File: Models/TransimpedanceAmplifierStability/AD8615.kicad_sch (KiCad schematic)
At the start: 10 parts

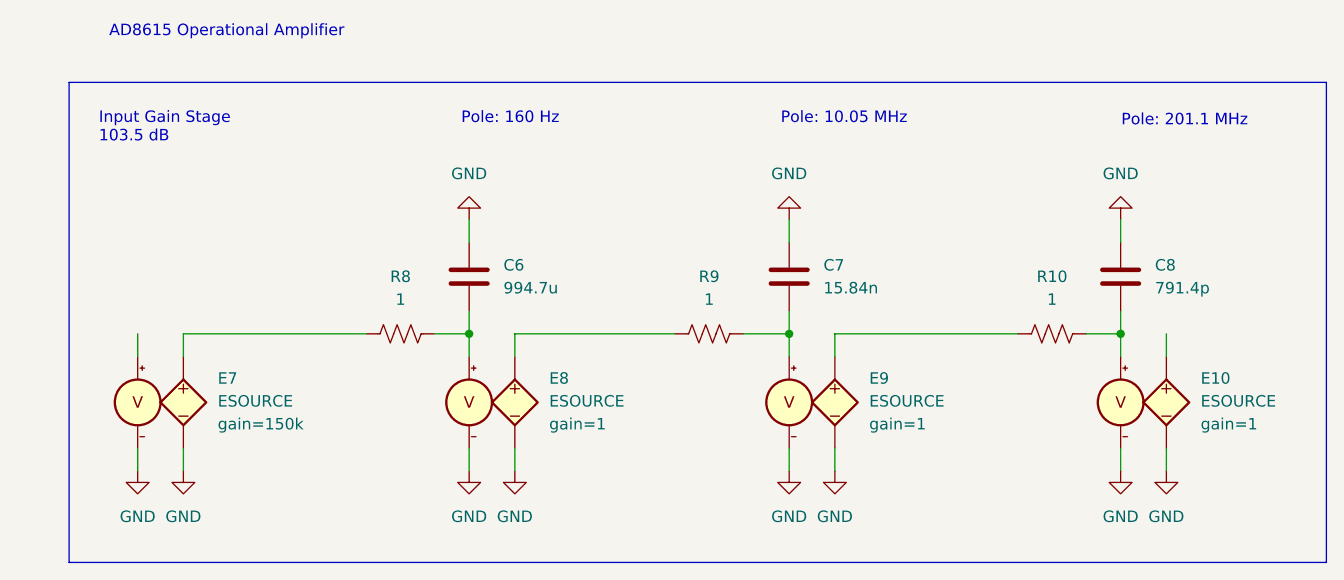
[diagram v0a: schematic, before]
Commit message: Upload completed model of the LTC6090-5
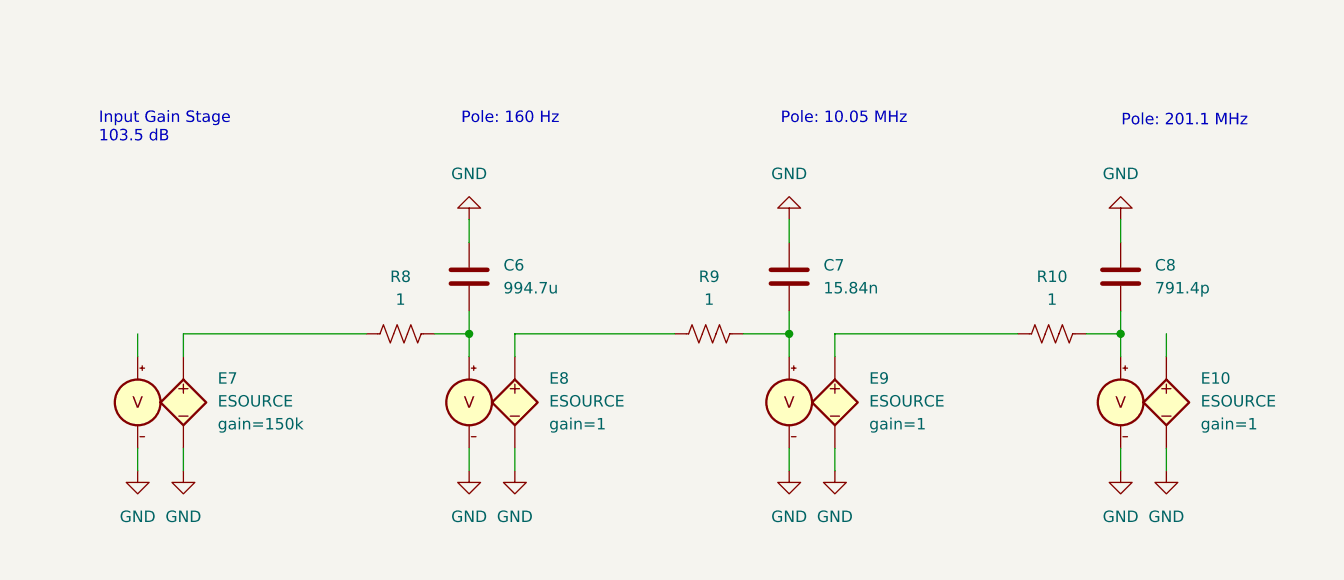
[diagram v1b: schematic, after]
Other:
- note removed: "AD8615 Operational Amplifier"
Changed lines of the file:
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@@
 	(generator_version "9.0")
 	(paper "A4")
-	(rectangle
-		(start 93.98 68.58)
-		(end 233.68 121.92)
-		(stroke
-			(width 0)
-			(type default)
-		)
-		(fill
-			(type none)
-		)
-	)
 	(text "Input Gain Stage\n103.5 dB"
 		(exclude_from_sim no)
@@
 		(effects
 			(font
-				(size 1.27 1.27)
-			)
-		)
-	)
-	(text "AD8615 Operational Amplifier"
-		(exclude_from_sim no)
-		(at 111.506 62.992 0)
-		(effects
-			(font

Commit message: Upload latest version of TIA stability KiCad project
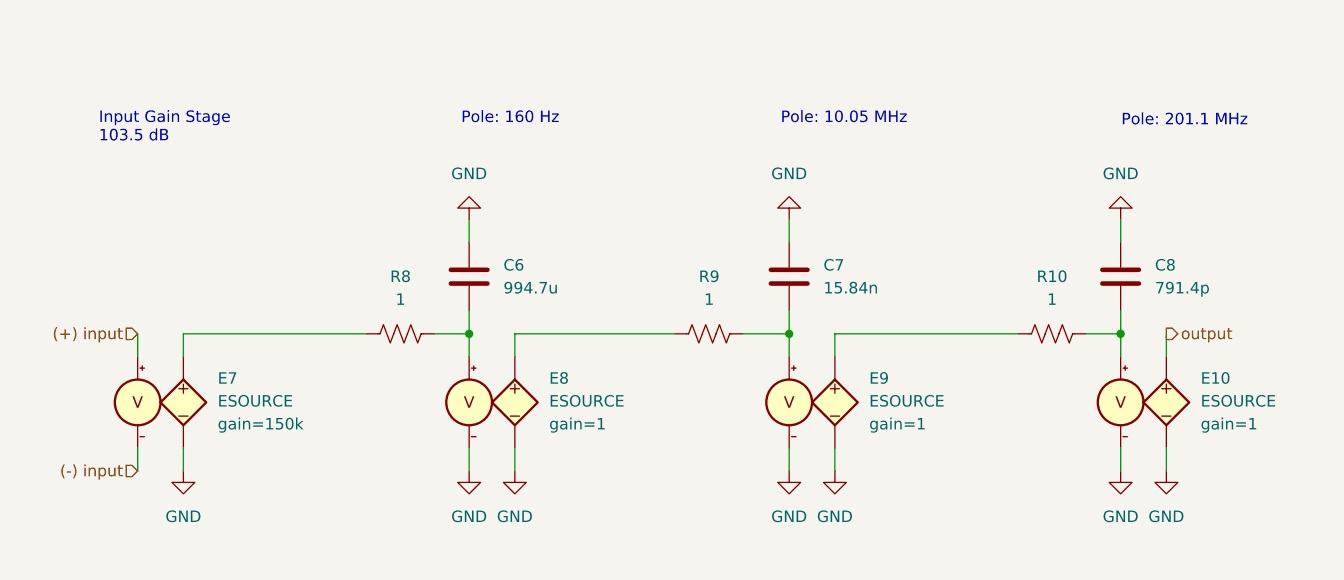
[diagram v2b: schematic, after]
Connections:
- net GND: no longer E7.4 (C-)
- net (+) input: now reaches E7.3 (C+)
- net output: now reaches E10.1 (N+)
- new net (-) input: E7.4 (C-)
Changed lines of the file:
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@@
+		)
+	)
+	(hierarchical_label "output"
+		(shape output)
+		(at 215.9 96.52 0)
+		(effects
+			(font
+				(size 1.27 1.27)
+			)
+			(justify left)
+		)
+	)
+	(hierarchical_label "(-) input"
+		(shape input)
+		(at 101.6 111.76 180)
+		(effects
+			(font
+				(size 1.27 1.27)
+			)
+			(justify right)
+		)
+	)
+	(hierarchical_label "(+) input"
+		(shape input)
+		(at 101.6 96.52 180)
+		(effects
+			(font
+				(size 1.27 1.27)
+			)
+			(justify right)
 		)
 	)
@@
 					(unit 1)
 				)
+				(path "/b282eeea-1083-4bd9-aef5-c78f2e129a69/83a2ffcb-675c-4711-b7ba-b056f35f4220"
+					(reference "#PWR035")
+					(unit 1)
+				)
 			)
 		)
@@
 					(unit 1)
 				)
+				(path "/b282eeea-1083-4bd9-aef5-c78f2e129a69/83a2ffcb-675c-4711-b7ba-b056f35f4220"
+					(reference "E12")
+					(unit 1)
+				)
 			)
 		)
@@
 					(unit 1)
 				)
+				(path "/b282eeea-1083-4bd9-aef5-c78f2e129a69/83a2ffcb-675c-4711-b7ba-b056f35f4220"
+					(reference "#PWR039")
+					(unit 1)
+				)
 			)
 		)
@@
 					(unit 1)
 				)
+				(path "/b282eeea-1083-4bd9-aef5-c78f2e129a69/83a2ffcb-675c-4711-b7ba-b056f35f4220"
+					(reference "#PWR034")
+					(unit 1)
+				)
 			)
 		)
@@
 					(unit 1)
 				)
+				(path "/b282eeea-1083-4bd9-aef5-c78f2e129a69/83a2ffcb-675c-4711-b7ba-b056f35f4220"
+					(reference "C9")
+					(unit 1)
+				)
 			)
 		)
@@
 					(unit 1)
 				)
+				(path "/b282eeea-1083-4bd9-aef5-c78f2e129a69/83a2ffcb-675c-4711-b7ba-b056f35f4220"
+					(reference "R11")
+					(unit 1)
+				)
 			)
 		)
@@
 					(unit 1)
 				)
+				(path "/b282eeea-1083-4bd9-aef5-c78f2e129a69/83a2ffcb-675c-4711-b7ba-b056f35f4220"
+					(reference "#PWR05")
+					(unit 1)
+				)
 			)
 		)
@@
 					(unit 1)
 				)
+				(path "/b282eeea-1083-4bd9-aef5-c78f2e129a69/83a2ffcb-675c-4711-b7ba-b056f35f4220"
+					(reference "#PWR041")
+					(unit 1)
+				)
 			)
 		)
@@
 					(unit 1)
 				)
+				(path "/b282eeea-1083-4bd9-aef5-c78f2e129a69/83a2ffcb-675c-4711-b7ba-b056f35f4220"
+					(reference "#PWR040")
+					(unit 1)
+				)
 			)
 		)
@@
 					(unit 1)
 				)
+				(path "/b282eeea-1083-4bd9-aef5-c78f2e129a69/83a2ffcb-675c-4711-b7ba-b056f35f4220"
+					(reference "#PWR036")
+					(unit 1)
+				)
 			)
 		)
@@
 					(unit 1)
 				)
+				(path "/b282eeea-1083-4bd9-aef5-c78f2e129a69/83a2ffcb-675c-4711-b7ba-b056f35f4220"
+					(reference "E11")
+					(unit 1)
+				)
 			)
 		)
@@
 					(unit 1)
 				)
+				(path "/b282eeea-1083-4bd9-aef5-c78f2e129a69/83a2ffcb-675c-4711-b7ba-b056f35f4220"
+					(reference "#PWR038")
+					(unit 1)
+				)
 			)
 		)
@@
 					(unit 1)
 				)
+				(path "/b282eeea-1083-4bd9-aef5-c78f2e129a69/83a2ffcb-675c-4711-b7ba-b056f35f4220"
+					(reference "R12")
+					(unit 1)
+				)
 			)
 		)
@@
 					(unit 1)
 				)
-			)
-		)
-	)
-	(symbol
-		(lib_id "power:GND")
-		(at 101.6 111.76 0)
-		(unit 1)
-		(exclude_from_sim no)
-		(in_bom yes)
-		(on_board yes)
-		(dnp no)
-		(fields_autoplaced yes)
-		(property "Reference" "#PWR07"
-			(at 101.6 118.11 0)
-			(effects
-				(font
-					(size 1.27 1.27)
-				)
-				(hide yes)
-			)
-		)
-		(property "Value" "GND"
-			(at 101.6 116.84 0)
-			(effects
-				(font
-					(size 1.27 1.27)
-				)
-			)
-		)
-		(property "Footprint" ""
-			(at 101.6 111.76 0)
-			(effects
-				(font
-					(size 1.27 1.27)
-				)
-				(hide yes)
-			)
-		)
-		(property "Datasheet" ""
-			(at 101.6 111.76 0)
-			(effects
-				(font
-					(size 1.27 1.27)
-				)
-				(hide yes)
-			)
-		)
-		(property "Description" "Power symbol creates a global label with name \"GND\" , ground"
-			(at 101.6 111.76 0)
-			(effects
-				(font
-					(size 1.27 1.27)
-				)
-				(hide yes)
-			)
-		)
-		(pin "1"
-		)
-		(instances
-			(project "TransimpedanceAmplifierStability"
-				(path "/b282eeea-1083-4bd9-aef5-c78f2e129a69/350a7392-f8dd-4a96-b4e8-c2f5595b2b98"
-					(reference "#PWR07")
+				(path "/b282eeea-1083-4bd9-aef5-c78f2e129a69/83a2ffcb-675c-4711-b7ba-b056f35f4220"
+					(reference "#PWR037")
 					(unit 1)
 				)
@@
 					(unit 1)
 				)
+				(path "/b282eeea-1083-4bd9-aef5-c78f2e129a69/83a2ffcb-675c-4711-b7ba-b056f35f4220"
+					(reference "E14")
+					(unit 1)
+				)
 			)
 		)
@@
 					(unit 1)
 				)
+				(path "/b282eeea-1083-4bd9-aef5-c78f2e129a69/83a2ffcb-675c-4711-b7ba-b056f35f4220"
+					(reference "R13")
+					(unit 1)
+				)
 			)
 		)
@@
 					(unit 1)
 				)
+				(path "/b282eeea-1083-4bd9-aef5-c78f2e129a69/83a2ffcb-675c-4711-b7ba-b056f35f4220"
+					(reference "C10")
+					(unit 1)
+				)
 			)
 		)
@@
 					(unit 1)
 				)
+				(path "/b282eeea-1083-4bd9-aef5-c78f2e129a69/83a2ffcb-675c-4711-b7ba-b056f35f4220"
+					(reference "#PWR042")
+					(unit 1)
+				)
 			)
 		)
@@
 					(unit 1)
 				)
+				(path "/b282eeea-1083-4bd9-aef5-c78f2e129a69/83a2ffcb-675c-4711-b7ba-b056f35f4220"
+					(reference "E13")
+					(unit 1)
+				)
 			)
 		)
@@
 					(unit 1)
 				)
+				(path "/b282eeea-1083-4bd9-aef5-c78f2e129a69/83a2ffcb-675c-4711-b7ba-b056f35f4220"
+					(reference "C11")
+					(unit 1)
+				)
